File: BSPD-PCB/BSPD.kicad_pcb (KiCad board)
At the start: 2 copper layers, 77 x 54 mm, 79 parts, among them J1 Conn_01x03_Socket, J2 Conn_01x03_Socket, J3 Conn_01x02_Socket, J4 Conn_01x02_Socket, K1 Relay_SPST-NO, Q1 2N7002, Q2 2N7002, U1 LM393, U2 LM393, U3 TPS7B88-Q1, U4 74LVC1G11, U5 74LVC1G332, U6 LTC6994xS6-1, U7 LTC6994xS6-1, U8 74LVC1G332

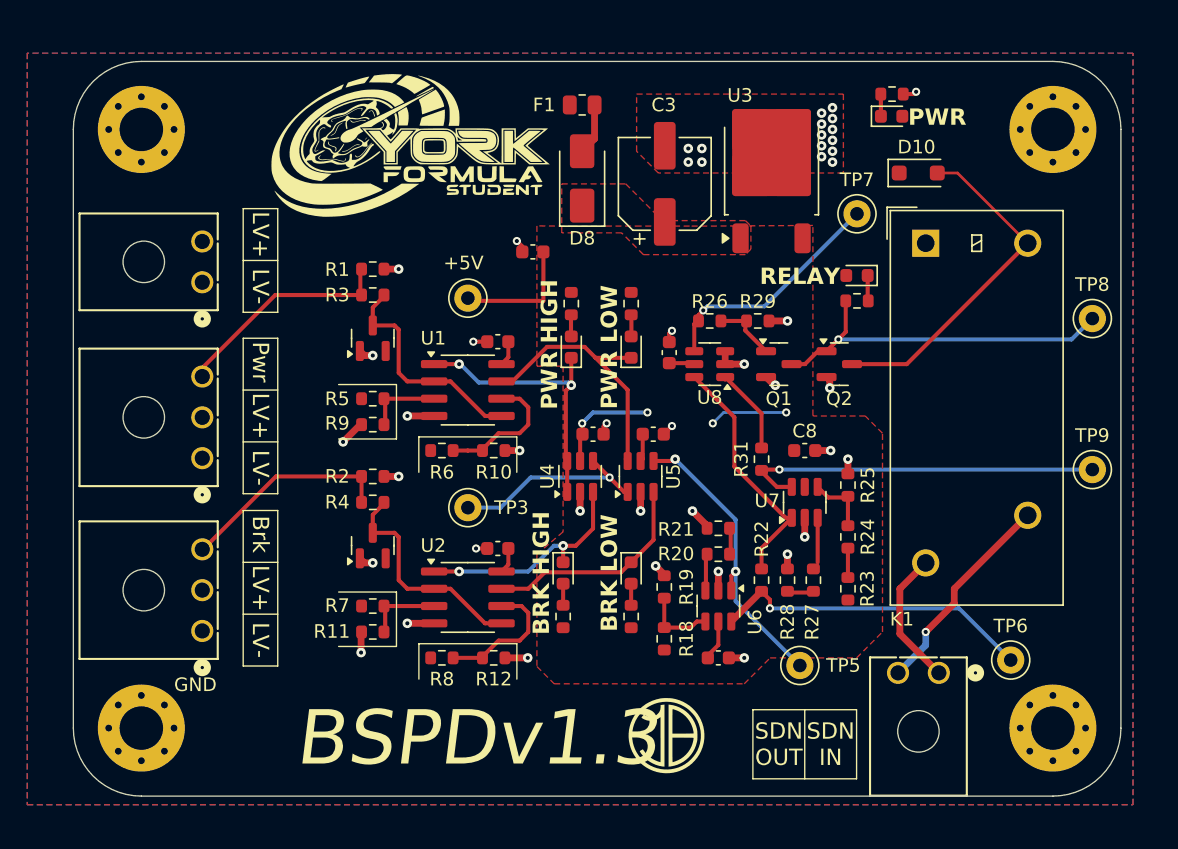
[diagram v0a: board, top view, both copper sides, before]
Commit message: Updated production gerbers
Reversed shutdown connector
Added back test points 1 and 2
Fixed shutdown connector placement
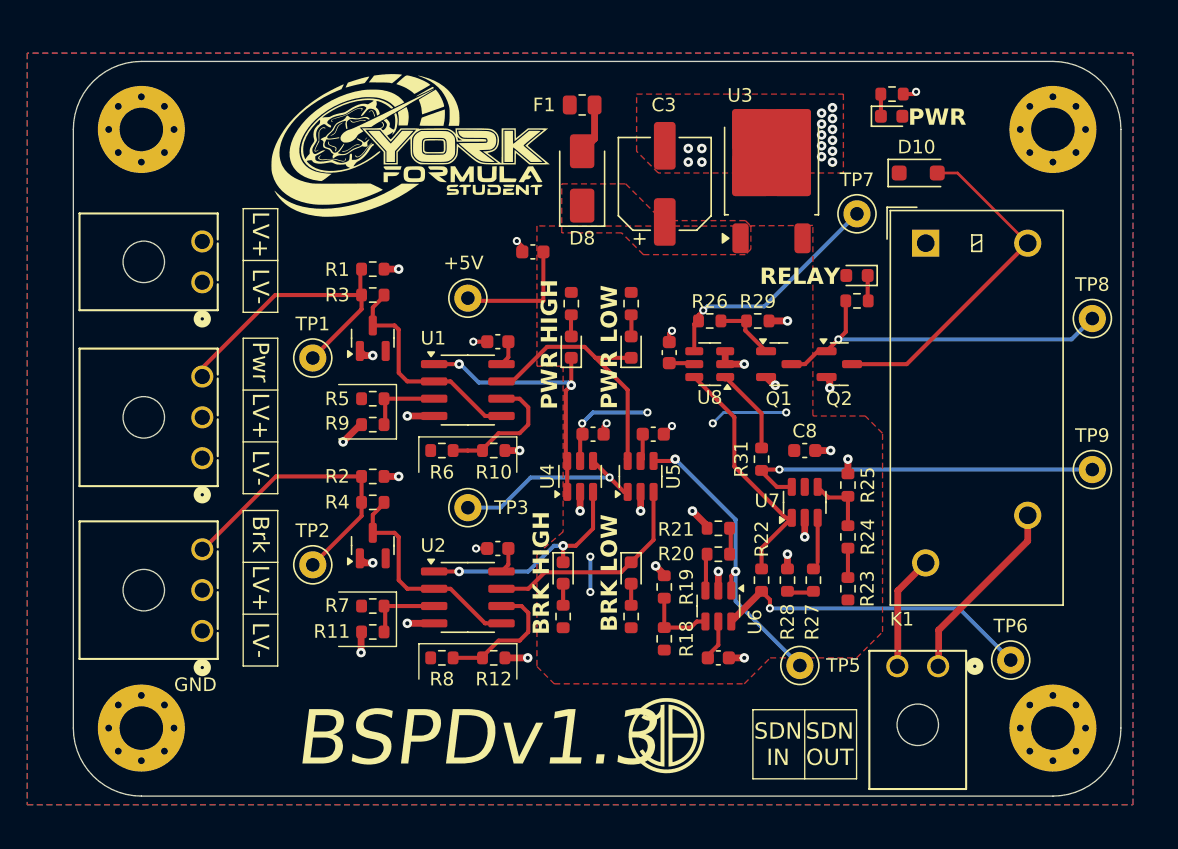
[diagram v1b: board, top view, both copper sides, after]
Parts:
- added TP1: TestPoint, TestPoint:TestPoint_Keystone_5000-5004_Miniature, F.Cu at (75.6, 94.8)
- added TP2: TestPoint, TestPoint:TestPoint_Keystone_5000-5004_Miniature, F.Cu at (75.6, 110.0)
- moved J4 0.49 mm to (121.6, 117.5)
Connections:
- J4 pad 1: Shutdown In -> Shutdown Out
- J4 pad 2: Shutdown Out -> Shutdown In
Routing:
- net Sensor 1 Input: track 16.5 -> 22.6 mm
- net Sensor 2 Input: track 15.7 -> 21.8 mm
- net +5V: track 30.2 -> 32.8 mm, vias 4 -> 6
- net Shutdown Out: track 15.5 -> 13.8 mm, vias 1 -> 0
- net Shutdown In: track 10.1 -> 8.58 mm

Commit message: V1.4
Replaced Comparators for push pull (not yet selected)
Changed input block to 5V
Added more test points
Changed Zener Package
Moved Diodes to active high
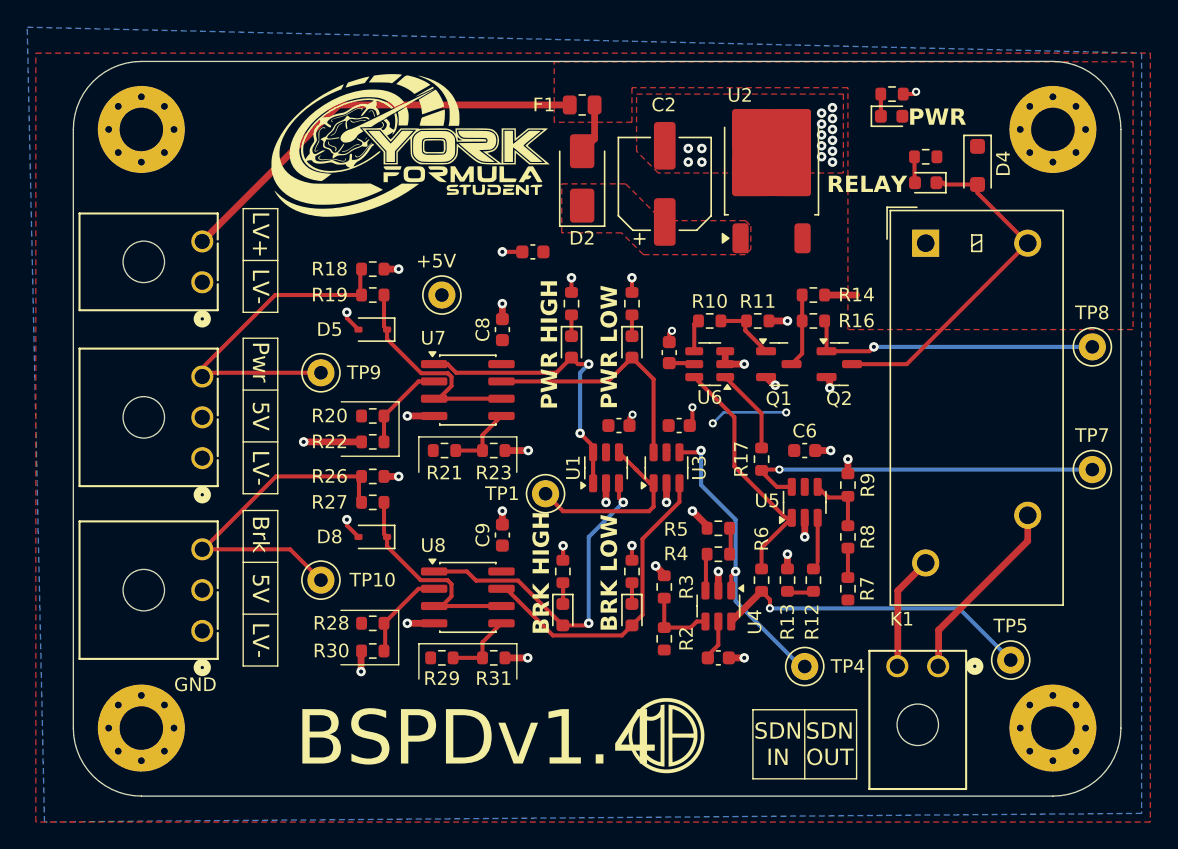
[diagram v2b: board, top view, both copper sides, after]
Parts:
- removed the C1 at (89.2, 93.6)
- removed the C2 at (89.2, 108.8)
- removed the D1 at (80.0, 93.3)
- removed the D2 at (80.0, 108.6)
- removed the D4 at (94.6, 94.0)
- removed the R1 at (80.0, 88.3)
- removed the R10 at (88.9, 101.6)
- removed the R11 at (80.0, 114.9)
- removed the R12 at (88.9, 116.8)
- removed the R17 at (99.0, 113.8)
- removed the R2 at (80.0, 103.5)
- removed the R3 at (80.0, 90.2)
- removed the R4 at (80.0, 105.4)
- removed the R5 at (80.0, 97.8)
- removed the R6 at (85.1, 101.6)
- removed the R7 at (80.0, 113.0)
- removed the R8 at (85.1, 116.8)
- removed the R9 at (80.0, 99.7)
- removed TP2: TestPoint, TestPoint:TestPoint_Keystone_5000-5004_Miniature
- removed the TP5 at (111.4, 117.4)
- removed the TP7 at (115.6, 84.2)
- removed the U1 at (87.0, 97.2)
- removed the U2 at (87.0, 112.4)
- added C8: 1µ, Capacitor_SMD:C_0603_1608Metric, F.Cu at (89.5, 92.7)
- added C9: 1µ, Capacitor_SMD:C_0603_1608Metric, F.Cu at (89.5, 107.8)
- added D10: LED, LED_SMD:LED_0603_1608Metric, F.Cu at (99.1, 113.7)
- added D3: LED, LED_SMD:LED_0603_1608Metric, F.Cu at (120.7, 81.9)
- added D8: BZX384xxxx, Diode_SMD:D_SOD-323, F.Cu at (80.0, 108.0)
- added R18: 10k, Resistor_SMD:R_0603_1608Metric, F.Cu at (80.0, 88.3)
- added R19: 4.8k, Resistor_SMD:R_0603_1608Metric, F.Cu at (80.0, 90.2)
- added R20: 39K, Resistor_SMD:R_0603_1608Metric, F.Cu at (80.0, 99.1)
- added R21: 39K, Resistor_SMD:R_0603_1608Metric, F.Cu at (85.3, 101.6)
- added R22: 62k, Resistor_SMD:R_0603_1608Metric, F.Cu at (80.0, 101.0)
- added R23: 62k, Resistor_SMD:R_0603_1608Metric, F.Cu at (88.9, 101.6)
- added R24: R, Resistor_SMD:R_0603_1608Metric, F.Cu at (94.6, 90.8)
- added R25: R, Resistor_SMD:R_0603_1608Metric, F.Cu at (99.1, 90.8)
- added R26: 10k, Resistor_SMD:R_0603_1608Metric, F.Cu at (80.0, 103.5)
- added R27: 4.8k, Resistor_SMD:R_0603_1608Metric, F.Cu at (80.0, 105.4)
- added R28: 39K, Resistor_SMD:R_0603_1608Metric, F.Cu at (80.0, 114.3)
- added R29: 39K, Resistor_SMD:R_0603_1608Metric, F.Cu at (85.1, 116.8)
- added R31: 62k, Resistor_SMD:R_0603_1608Metric, F.Cu at (88.9, 116.8)
- added R32: R, Resistor_SMD:R_0603_1608Metric, F.Cu at (94.0, 110.5)
- added R33: R, Resistor_SMD:R_0603_1608Metric, F.Cu at (99.1, 110.5)
- added TP10: TestPoint, TestPoint:TestPoint_Keystone_5000-5004_Miniature, F.Cu at (76.2, 111.1)
- added TP9: TestPoint, TestPoint:TestPoint_Keystone_5000-5004_Miniature, F.Cu at (76.2, 95.9)
- added U7: LM393, Package_SO:SOIC-8_3.9x4.9mm_P1.27mm, F.Cu at (87.0, 97.2)
- added U8: LM393, Package_SO:SOIC-8_3.9x4.9mm_P1.27mm, F.Cu at (87.0, 112.4)
- D5: value LED -> BZX384xxxx; footprint LED_SMD:LED_0603_1608Metric -> Diode_SMD:D_SOD-323
- R14: value 10K -> 10k
- R15: value 10K -> R
- R16: value 10K -> 200
- R30: value 10k -> 62k
- moved R30 43.9 mm to (80.0, 116.3)
- moved TP4 36.7 mm to (111.8, 117.5)
- moved D9 33.0 mm to (94.0, 113.7), turned to -90 degrees
- moved R16 28.5 mm to (112.4, 92.1), turned to 0 degrees
- moved R15 24.2 mm to (120.7, 80.0), turned to 180 degrees
- moved TP1 19.8 mm to (92.7, 104.8)
- moved D5 19.0 mm to (80.0, 92.7), turned to 180 degrees
- moved R14 17.8 mm to (112.4, 90.2), turned to 180 degrees
- moved D6 16.6 mm to (94.6, 94.0)
- moved D7 16.6 mm to (99.1, 94.0)
- moved TP3 15.7 mm to (85.1, 90.2)
- moved D4 4.40 mm to (124.5, 80.6), turned to -90 degrees
- moved TP8 2.08 mm to (132.9, 94.0)
- moved C1 2.01 mm to (98.1, 99.8)
- moved C3 2.01 mm to (102.5, 99.8)
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- renumbered C4 to C1, C3 to C2, C6 to C3, C5 to C4, C7 to C5, C8 to C6, C9 to C7, D3 to D1, D8 to D2, D10 to D4, R13 to R1, R26 to R10, R29 to R11, R27 to R12, R28 to R13, R31 to R17, R18 to R2, R19 to R3, R20 to R4, R21 to R5, R22 to R6, R23 to R7, R24 to R8, R25 to R9, TP6 to TP5, TP9 to TP7, U4 to U1, U3 to U2, U5 to U3, U6 to U4, U7 to U5, U8 to U6
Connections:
- D5 pad 1: /S1L -> Net-(D5-K)
- D5 pad 2: Net-(D5-A) -> GND
- D6 pad 1: /S2H -> Net-(D6-K)
- D6 pad 2: Net-(D6-A) -> /PWR_H
- D7 pad 1: /S2L -> Net-(D7-K)
- D7 pad 2: Net-(D7-A) -> /PWR_L
- D9 pad 2: +12V -> /BRK_H
- J1 pad 2: +12V -> +5V
- J1 pad 3: Sensor 1 Input -> PWR Input
- J2 pad 2: +12V -> +5V
- J2 pad 3: Sensor 2 Input -> Brake Input
- Q2 pad 1: Net-(Q1-D) -> Net-(Q2-G)
- R14 pad 1: Net-(D4-A) -> +12V
- R14 pad 2: +5V -> Net-(Q1-D)
- R15 pad 1: +5V -> +12V
- R15 pad 2: Net-(D5-A) -> Net-(D3-A)
- R16 pad 1: Net-(D6-A) -> Net-(Q1-D)
- R16 pad 2: +5V -> Net-(Q2-G)
- R30 pad 1: Net-(D9-K) -> /Brk Comparator/HighDiv
- R30 pad 2: Net-(Q1-D) -> GND
- TP1 pad 1: Sensor 1 Input -> Net-(TP1-Pad1)
- TP3 pad 1: Net-(TP3-Pad1) -> +5V
- TP4 pad 1: +5V -> Net-(U4-IN)
- TP8 pad 1: Net-(Q1-D) -> Net-(Q2-G)
- U1 pad 1: /S1H -> /PWR_H
- U1 pad 3: /S2H -> /BRK_H
- U1 pad 4: Net-(TP3-Pad1) -> Net-(TP1-Pad1)
- U1 pad 6: /S1H -> /PWR_H
- U3 pad 1: Net-(TP3-Pad1) -> Net-(TP1-Pad1)
- U3 pad 3: /S2L -> /BRK_L
- U3 pad 4: Error Signal -> Net-(U4-IN)
- U3 pad 6: /S1L -> /PWR_L
- U4 pad 1: Error Signal -> Net-(U4-IN)
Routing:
- net +12V: track 3.76 -> 33.5 mm
- net Brake Input: track 0.00 -> 25.3 mm
- net PWR Input: track 0.00 -> 25.2 mm
- net /BRK_H: track 0.00 -> 24.5 mm, vias 0 -> 2
- net /BRK_L: track 0.00 -> 23.2 mm
- net Sensor 1 Input: track 22.6 -> 0.00 mm
- net Error Signal: track 22.1 -> 0.00 mm, vias 2 -> 0
- net Net-(U4-IN): track 0.00 -> 22.0 mm, vias 0 -> 2
- net Net-(Q2-G): track 0.00 -> 22.0 mm, vias 0 -> 1
- net Sensor 2 Input: track 21.8 -> 0.00 mm
- net +5V: track 32.8 -> 11.1 mm, vias 6 -> 2
- net /PWR_H: track 0.00 -> 21.7 mm, vias 0 -> 2
- net Net-(Q1-D): track 26.2 -> 5.40 mm, vias 1 -> 0
- net /S1H: track 20.8 -> 0.00 mm, vias 2 -> 0
- net /S1L: track 19.7 -> 0.00 mm
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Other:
- board text added: "5V"
- board text added: "BSPDv1.4"
- board text removed: "BSPDv1.3"
